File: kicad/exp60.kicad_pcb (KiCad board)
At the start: 2 copper layers, 285.8 x 95.2 mm, 152 parts, among them K0 KEYSW, K1 KEYSW, K10 KEYSW, K11 KEYSW, K12 KEYSW, K13 KEYSW, K14 KEYSW, K15 KEYSW, K16 KEYSW, K17 KEYSW, K18 KEYSW, K19 KEYSW, K2 KEYSW, K20 KEYSW, K21 KEYSW, K22 KEYSW, K23 KEYSW, K24 KEYSW, K25 KEYSW, K26 KEYSW, K27 KEYSW, K28 KEYSW, K29 KEYSW, K3 KEYSW, K30 KEYSW, K31 KEYSW, K32 KEYSW, K33 KEYSW, K34 KEYSW, K35 KEYSW, K36 KEYSW, K37 KEYSW, K38 KEYSW, K39 KEYSW, K4 KEYSW, K40 KEYSW, K41 KEYSW, K42 KEYSW, K43 KEYSW, K44 KEYSW, K45 KEYSW, K46 KEYSW, K47 KEYSW, K48 KEYSW, K49 KEYSW, K5 KEYSW, K50 KEYSW, K51 KEYSW, K52 KEYSW, K53 KEYSW, K54 KEYSW, K55 KEYSW, K56 KEYSW, K57 KEYSW, K58 KEYSW, K59 KEYSW, K6 KEYSW, K60 KEYSW, K61 KEYSW, K62 KEYSW, K63 KEYSW, K64 KEYSW, K7 KEYSW, K8 KEYSW, K9 KEYSW, SW0 Reset, U0 ATmega32U2, U1 PRTR5V0U2X, Y0 16MHz

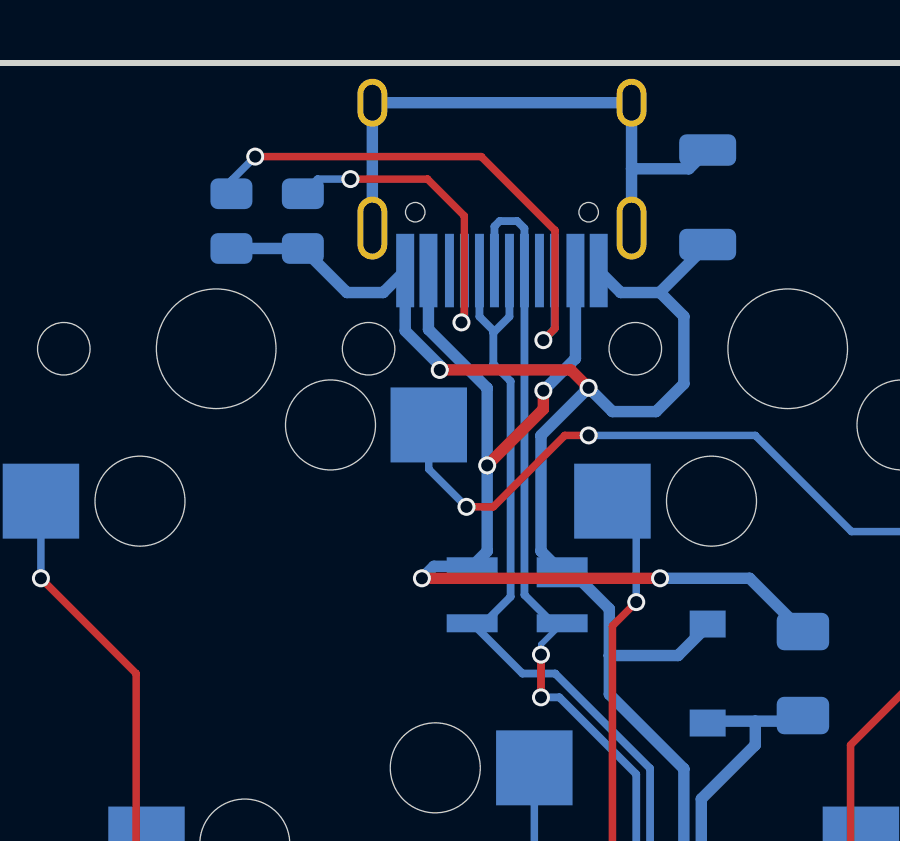
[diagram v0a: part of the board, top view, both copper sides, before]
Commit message: replace usb receptacle
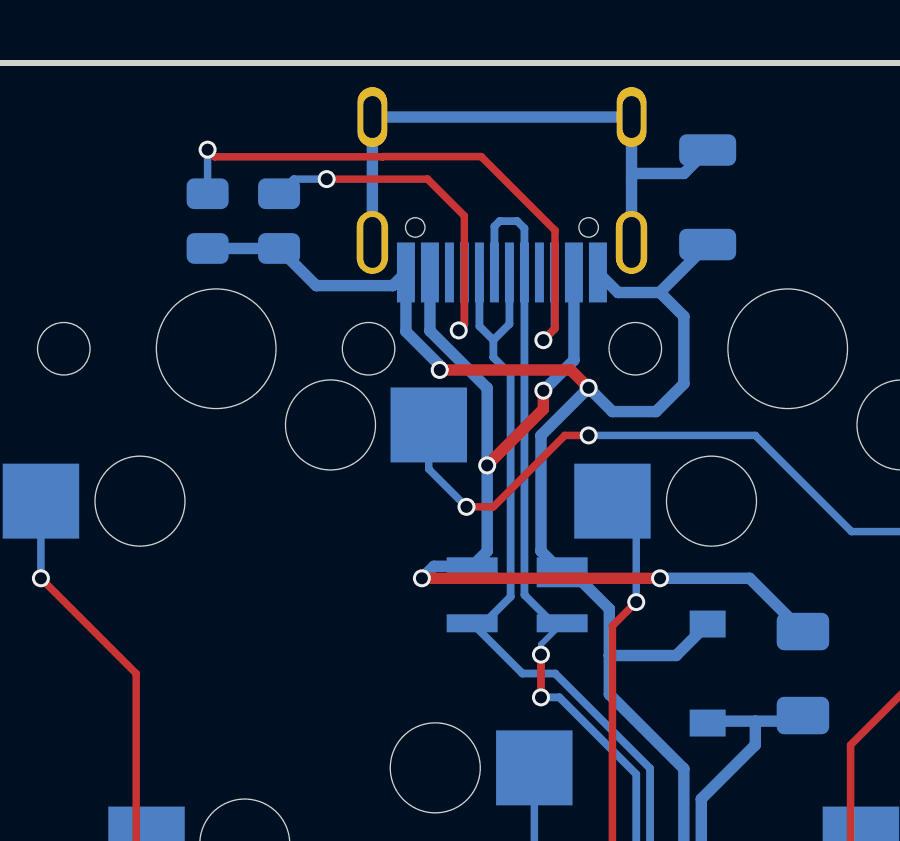
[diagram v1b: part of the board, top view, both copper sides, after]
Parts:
- removed D65: SMF6.0CA, Diode_SMD:D_SOD-123
- removed F0: Polyfuse_Small, Fuse:Fuse_1206_3216Metric
- removed R1, R2: 5.1k, Resistor_SMD:R_0805_2012Metric
- removed USB0: HRO-TYPE-C-31-M-12, Type-C:HRO-TYPE-C-31-M-12-HandSoldering
- added D66: SMF6.0CA, Diode_SMD:D_SOD-123, B.Cu at (96.8, 104.0)
- added F1: Polyfuse_Small, Fuse:Fuse_1206_3216Metric, B.Cu at (100.0, 104.0)
- added J0: USB4105-GF-A, GCT_USB4105-GF-A:GCT_USB4105-GF-A-HandSoldering, B.Cu at (90.0, 85.4)
- added R6: 5.1k, Resistor_SMD:R_0805_2012Metric, B.Cu at (82.5, 88.9)
- added R7: 5.1k, Resistor_SMD:R_0805_2012Metric, B.Cu at (80.2, 88.9)
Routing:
- net Net-(J0-PadB5): track 0.00 -> 20.4 mm, vias 0 -> 2
- net Net-(R1-Pad2): track 18.9 -> 0.00 mm, vias 2 -> 0
- net Net-(J0-PadA5): track 0.00 -> 12.9 mm, vias 0 -> 2
- net Net-(R2-Pad2): track 11.6 -> 0.00 mm, vias 2 -> 0

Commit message: label and route cleanup
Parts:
- moved D41 37.6 mm to (137.3, 156.4), turned to 180 degrees
- moved D42 6.53 mm to (137.3, 153.4), turned to 180 degrees
- moved C3 0.29 mm to (156.4, 159.5)
- moved C4 0.29 mm to (158.8, 159.5)
- moved C5 0.29 mm to (161.1, 159.5)
- moved C6 0.29 mm to (163.5, 159.5)
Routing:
- net ROW0: track 319.5 -> 378.0 mm
- net ROW3: track 261.7 -> 223.2 mm, vias 4 -> 2
- net ROW1: track 293.0 -> 331.4 mm
- net Net-(D41-Pad2): track 5.68 -> 43.8 mm, vias 0 -> 2
- net ROW2: track 259.5 -> 278.2 mm
- net COL1: track 181.6 -> 171.3 mm, vias 8 -> 7
- net Net-(D42-Pad2): track 5.68 -> 11.6 mm
- net COL12: track 248.2 -> 242.5 mm
- net COL6: track 123.8 -> 118.3 mm
- net COL11: track 224.4 -> 219.9 mm
- net Net-(D58-Pad2): track 53.9 -> 49.4 mm
- net COL9: track 171.8 -> 167.3 mm
- net COL8: track 154.4 -> 149.9 mm
- net COL4: track 120.6 -> 116.1 mm
- net COL10: track 204.8 -> 200.3 mm
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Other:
- board text added: "exp60 by Christian Schulze"
